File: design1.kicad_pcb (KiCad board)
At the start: 2 copper layers, 56.8 x 7.8 mm, 1 part

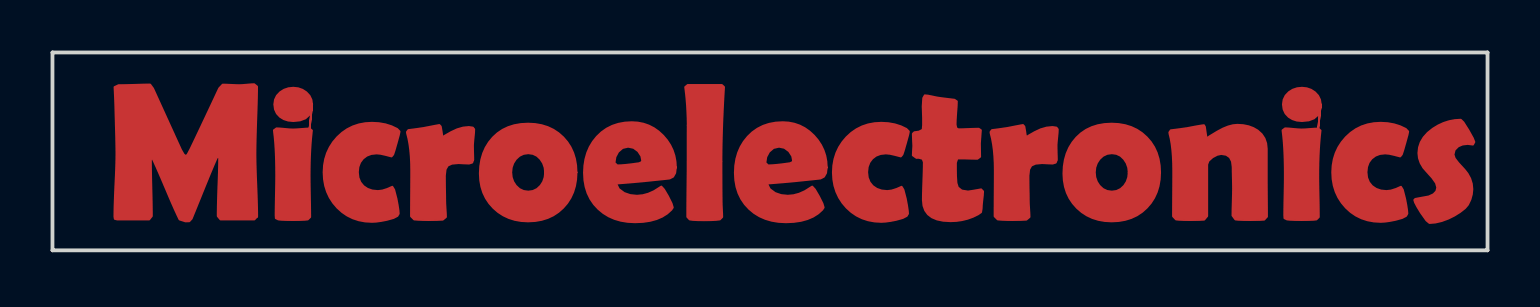
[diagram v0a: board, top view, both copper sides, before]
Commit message: Shorten the word ME.
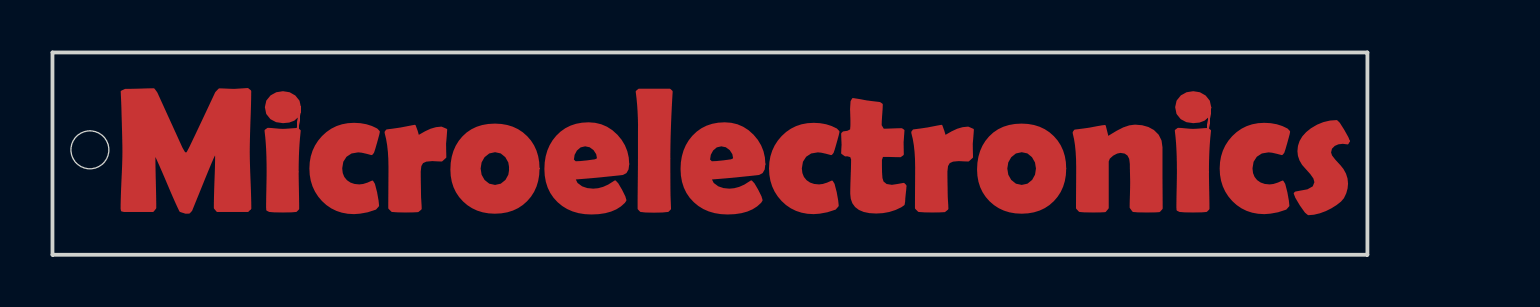
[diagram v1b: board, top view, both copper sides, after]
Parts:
- removed ME_Logo: G***, ME_BOLD:ME_Bold
- added REF**: Via(0.435-0.3mm), VIA:Via(0.435-0.3mm), F.Cu at (128.2, 103.1)
- added svg2mod: G***, ME_BOLD:ME_Bold, F.Cu at (153.8, 103.2)
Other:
- board size 56.8 x 7.8 mm -> 52 x 8 mm

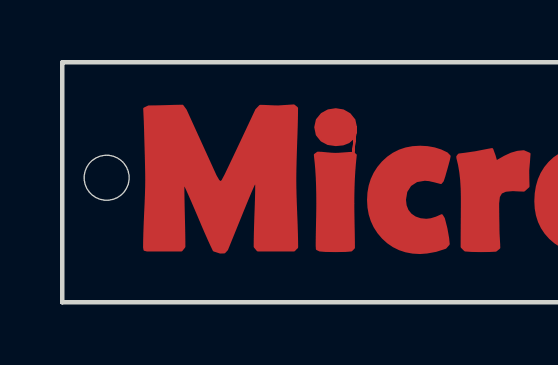
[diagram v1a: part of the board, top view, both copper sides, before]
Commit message: Move the drill hole upward and generated gerber files
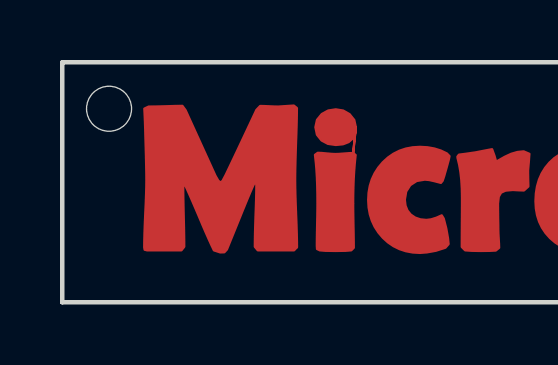
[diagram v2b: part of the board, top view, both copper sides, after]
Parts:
- moved REF** 2.30 mm to (128.3, 100.8)
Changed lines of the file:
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@@
     (links 0)
     (no_connects 0)
-    (area 126.674999 96.038394 183.575001 110.614006)
+    (area 118.444287 94.29 178.825001 110.26643)
     (thickness 1.6)
     (drawings 6)
@@
     (37 F.SilkS user hide)
     (38 B.Mask user hide)
-    (39 F.Mask user hide)
+    (39 F.Mask user)
     (40 Dwgs.User user hide)
     (41 Cmts.User user hide)
@@
     (visible_elements 7FFFFF7F)
     (pcbplotparams
-      (layerselection 0x01080_00000001)
+      (layerselection 0x010ff_80000001)
       (usegerberextensions true)
       (usegerberattributes true)
@@
   )
   (module "VIA:Via(0.435-0.3mm)" (layer F.Cu)
-    (at 128.23 103.1)
+    (at 128.31 100.8)
     (fp_text reference REF** (at 0.46 1.67) (layer F.SilkS) hide
       (effects (font (size 1 1) (thickness 0.15)))

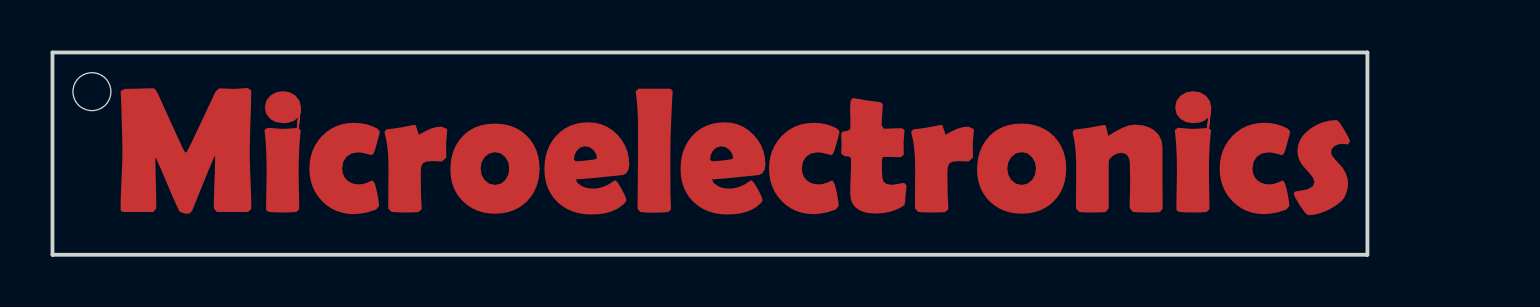
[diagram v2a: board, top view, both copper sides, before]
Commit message: Added another logo behind of it
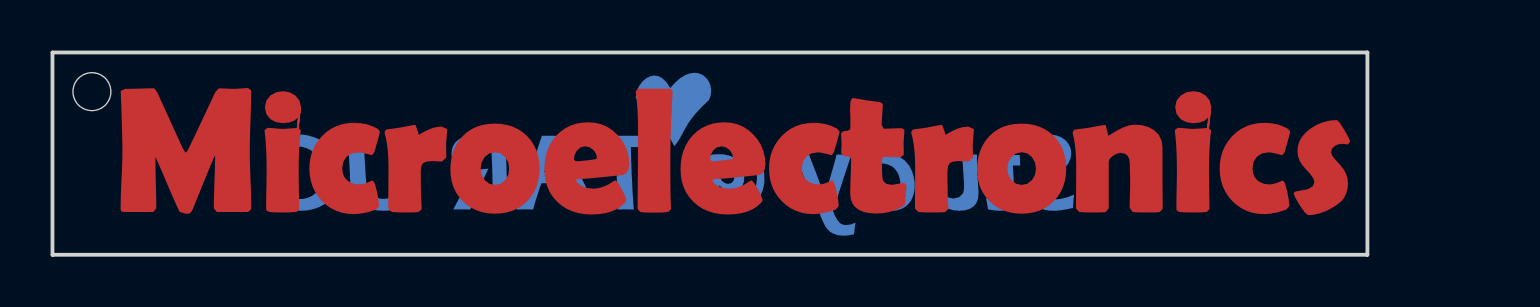
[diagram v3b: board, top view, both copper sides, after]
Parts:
- added Study@TARUC: G***, ME_BOLD:StudyAtTARUC, B.Cu at (151.4, 102.9)
